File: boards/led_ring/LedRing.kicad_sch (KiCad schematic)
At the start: 34 parts, among them J10 FH12-6S-0.5SH(55)

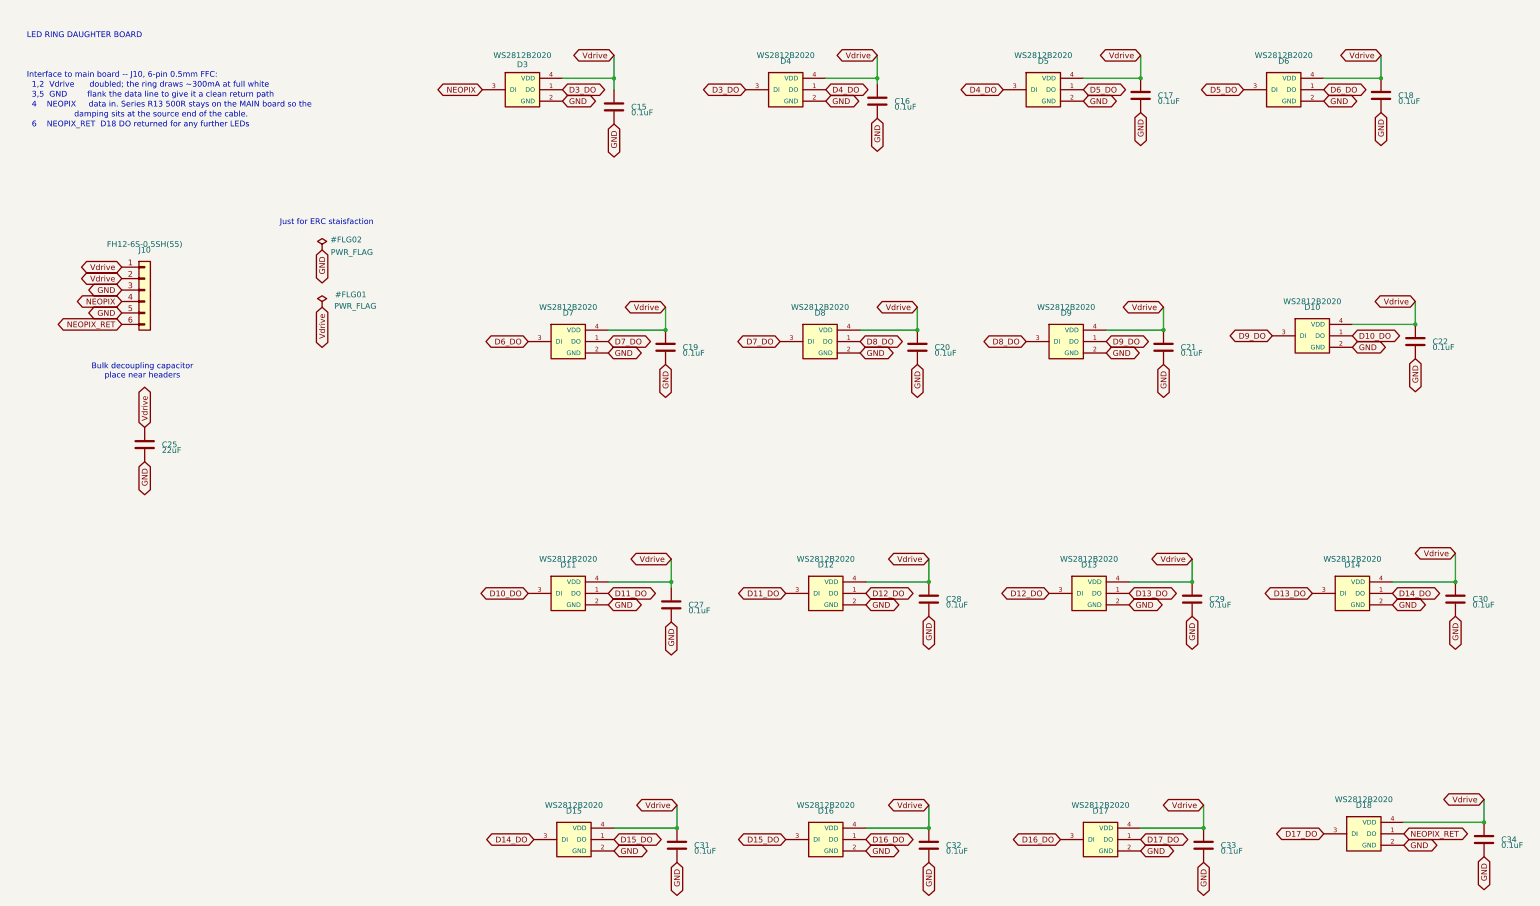
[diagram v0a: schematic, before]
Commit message: Board migrations. Move to newer LED and IMU
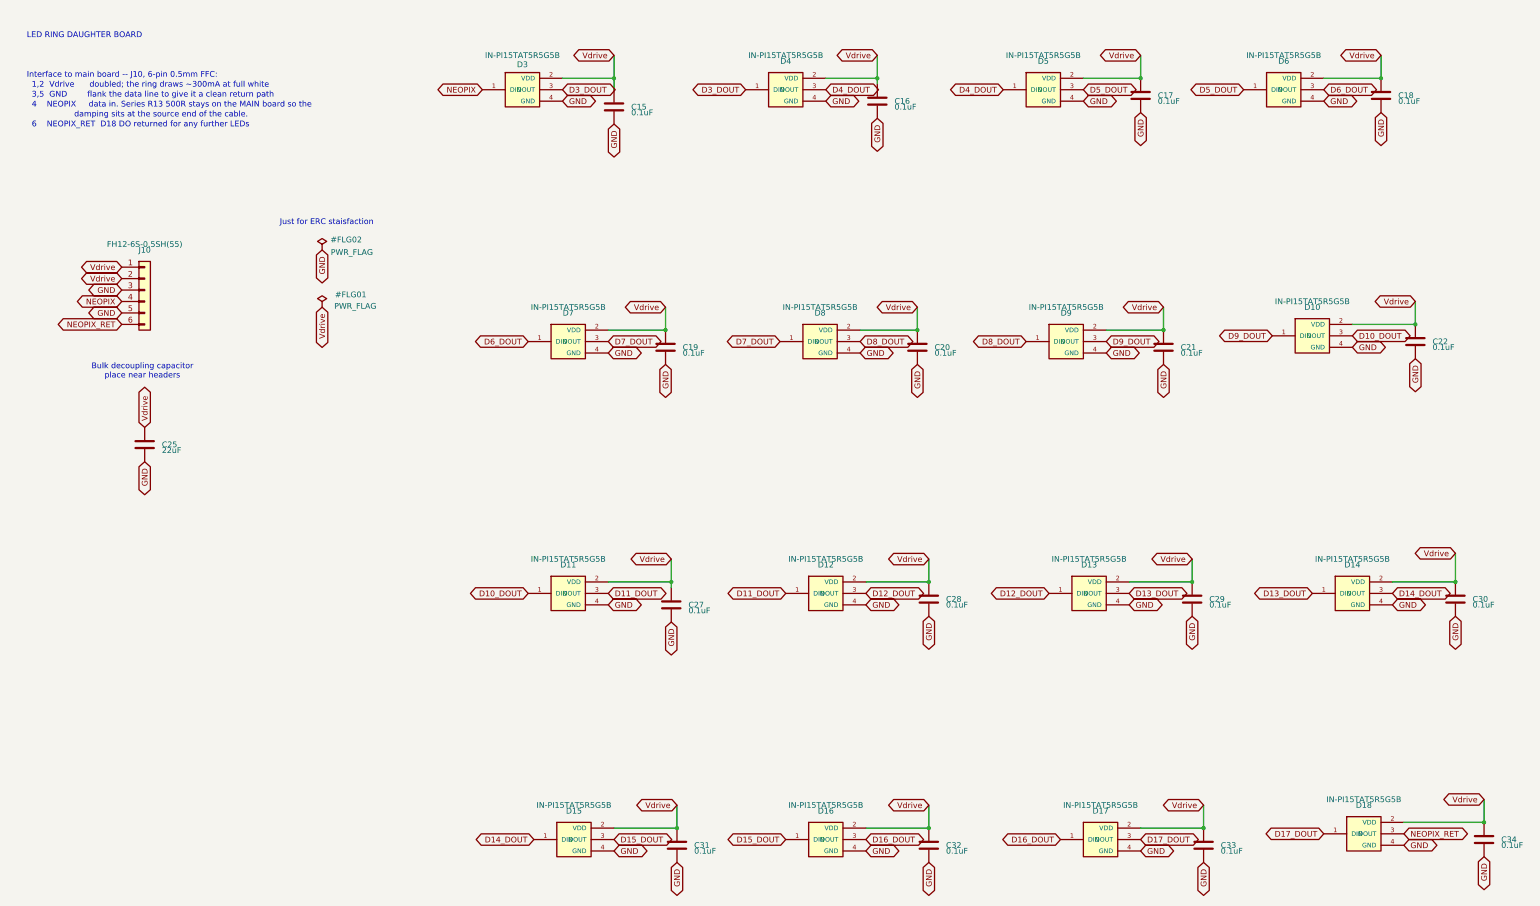
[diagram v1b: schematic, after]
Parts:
- C15, C16, C17, C18, C19, C20, C21, C22, C27, C28, C29, C30, C31, C32, C33, C34: Dielectric (none) -> X7R; DigiKey_PN (none) -> 1276-6844-1-ND; MPN (none) -> CL05B104KO5VPNC; Manufacturer (none) -> Samsung Electro-Mechanics; Voltage (none) -> 16V
- C25: Dielectric (none) -> X5R; DigiKey_PN (none) -> 1276-6786-1-ND; MPN (none) -> CL21A226KPCLRNC; Manufacturer (none) -> Samsung Electro-Mechanics; Voltage (none) -> 10V
- D10, D11, D12, D13, D14, D15, D16, D17, D4, D5, D6, D7, D8, D9: value WS2812B2020 -> IN-PI15TAT5R5G5B; footprint smart_compass:LED_WS2812B2020 -> smart_compass:LED_Inolux_IN-PI15TAT5R5G5B_1515; symbol smart_compass:WS2812B2020 -> smart_compass:IN-PI15TAT5R5G5B; DigiKey_PN (none) -> 1830-IN-PI15TAT5R5G5BCT-ND; MPN (none) -> IN-PI15TAT5R5G5B; Manufacturer (none) -> Inolux
- D18: value WS2812B2020 -> IN-PI15TAT5R5G5B; footprint smart_compass:LED_WS2812B2020 -> smart_compass:LED_Inolux_IN-PI15TAT5R5G5B_1515; symbol smart_compass:WS2812B2020 -> smart_compass:IN-PI15TAT5R5G5B; DigiKey_PN (none) -> 1830-IN-PI15TAT5R5G5BCT-ND; MPN (none) -> IN-PI15TAT5R5G5B; Manufacturer (none) -> Inolux; Sourcing_Note (none) -> Chain DOUT returns to the main board as NEOPIX_RET. The Ino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
- D3: value WS2812B2020 -> IN-PI15TAT5R5G5B; footprint smart_compass:LED_WS2812B2020 -> smart_compass:LED_Inolux_IN-PI15TAT5R5G5B_1515; symbol smart_compass:WS2812B2020 -> smart_compass:IN-PI15TAT5R5G5B; DigiKey_PN (none) -> 1830-IN-PI15TAT5R5G5BCT-ND; MPN (none) -> IN-PI15TAT5R5G5B; Manufacturer (none) -> Inolux; Sourcing_Note (none) -> V_IH is specified as 3.4V absolute at VDD=5.0V, NOT as a ra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
- J10: DigiKey_PN (none) -> HFJ106CT-ND; MPN (none) -> FH12-6S-0.5SH(55); Manufacturer (none) -> Hirose Electric Co Ltd; Sourcing_Note (none) -> Digi-Key stock 0, 16-week factory lead. Must be resolved to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
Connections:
- net GND: now also D10.4 (GND), D11.4 (GND), D12.4 (GND), D13.4 (GND), D14.4 (GND), D15.4 (GND), D16.4 (GND), D17.4 (GND), D18.4 (GND), D3.4 (GND), D4.4 (GND), D5.4 (GND), D6.4 (GND), D7.4 (GND), D8.4 (GND), D9.4 (GND); no longer D10.2 (GND), D11.2 (GND), D12.2 (GND), D13.2 (GND), D14.2 (GND), D15.2 (GND), D16.2 (GND), D17.2 (GND), D18.2 (GND), D3.2 (GND), D4.2 (GND), D5.2 (GND), D6.2 (GND), D7.2 (GND), D8.2 (GND), D9.2 (GND)
- net NEOPIX: now also D3.1 (DIN); no longer D3.3 (DI)
- net NEOPIX_RET: now also D18.3 (DOUT); no longer D18.1 (DO)
- net Vdrive: now also D10.2 (VDD), D11.2 (VDD), D12.2 (VDD), D13.2 (VDD), D14.2 (VDD), D15.2 (VDD), D16.2 (VDD), D17.2 (VDD), D18.2 (VDD), D3.2 (VDD), D4.2 (VDD), D5.2 (VDD), D6.2 (VDD), D7.2 (VDD), D8.2 (VDD), D9.2 (VDD); no longer D10.4 (VDD), D11.4 (VDD), D12.4 (VDD), D13.4 (VDD), D14.4 (VDD), D15.4 (VDD), D16.4 (VDD), D17.4 (VDD), D18.4 (VDD), D3.4 (VDD), D4.4 (VDD), D5.4 (VDD), D6.4 (VDD), D7.4 (VDD), D8.4 (VDD), D9.4 (VDD)
- net D10_DO renamed D11_DOUT
- net D11_DOUT: now also D12.1 (DIN); no longer D10.1 (DO)
- net D11_DO renamed D10_DOUT
- net D10_DOUT: now also D10.3 (DOUT); no longer D12.3 (DI)
- net D12_DO renamed D13_DOUT
- net D13_DOUT: now also D14.1 (DIN); no longer D12.1 (DO)
- net D13_DO renamed D12_DOUT
- net D12_DOUT: now also D12.3 (DOUT); no longer D14.3 (DI)
- net D14_DO renamed D15_DOUT
- net D15_DOUT: now also D16.1 (DIN); no longer D14.1 (DO)
- net D15_DO renamed D14_DOUT
- net D14_DOUT: now also D14.3 (DOUT); no longer D16.3 (DI)
- net D16_DO renamed D17_DOUT
- net D17_DOUT: now also D18.1 (DIN); no longer D16.1 (DO)
- net D17_DO renamed D16_DOUT
- net D16_DOUT: now also D16.3 (DOUT); no longer D18.3 (DI)
- net D3_DO renamed D4_DOUT
- net D4_DOUT: now also D5.1 (DIN); no longer D3.1 (DO)
- net D4_DO renamed D3_DOUT
- net D3_DOUT: now also D3.3 (DOUT); no longer D5.3 (DI)
- net D5_DO renamed D6_DOUT
- net D6_DOUT: now also D7.1 (DIN); no longer D5.1 (DO)
- net D6_DO renamed D5_DOUT
- net D5_DOUT: now also D5.3 (DOUT); no longer D7.3 (DI)
- net D7_DO renamed D8_DOUT
- net D8_DOUT: now also D9.1 (DIN); no longer D7.1 (DO)
- net D8_DO renamed D7_DOUT
- net D7_DOUT: now also D7.3 (DOUT); no longer D9.3 (DI)
- removed net D9_DO: D10.3 (DI), D9.1 (DO)
- new net D9_DOUT: D10.1 (DIN), D9.3 (DOUT)

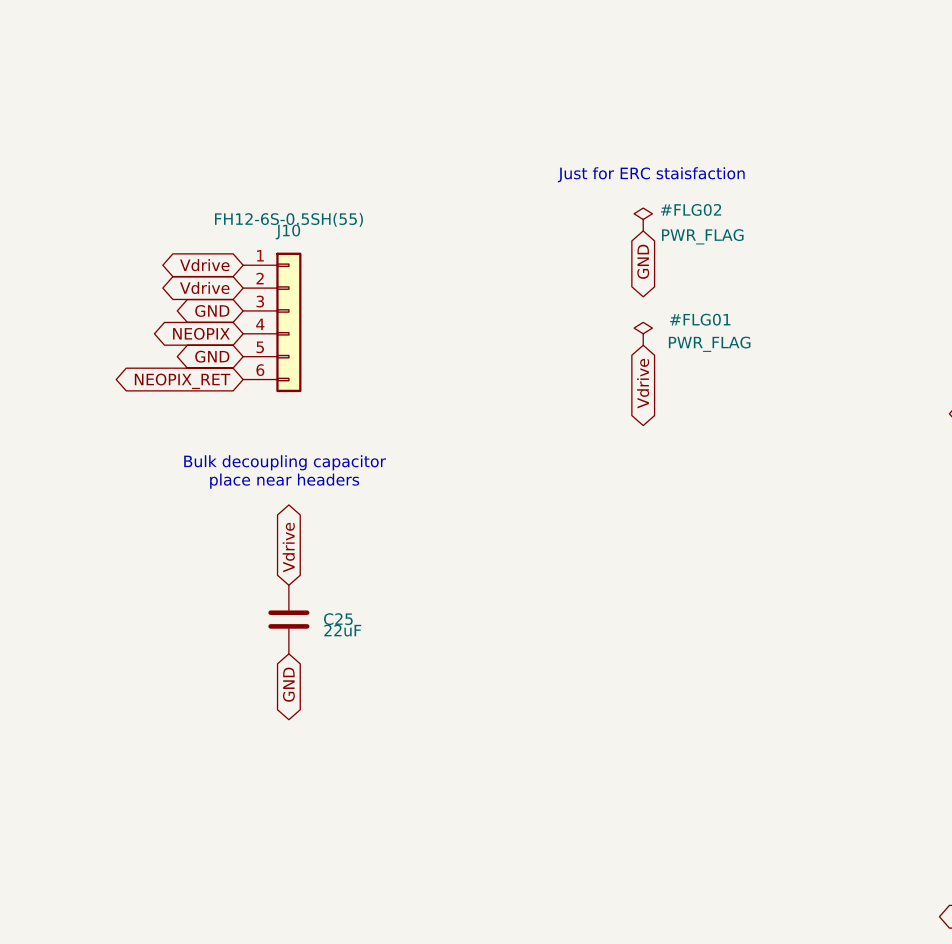
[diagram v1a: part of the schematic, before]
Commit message: some more component reworking. Moved to 10 lane ribbon connects between all boards
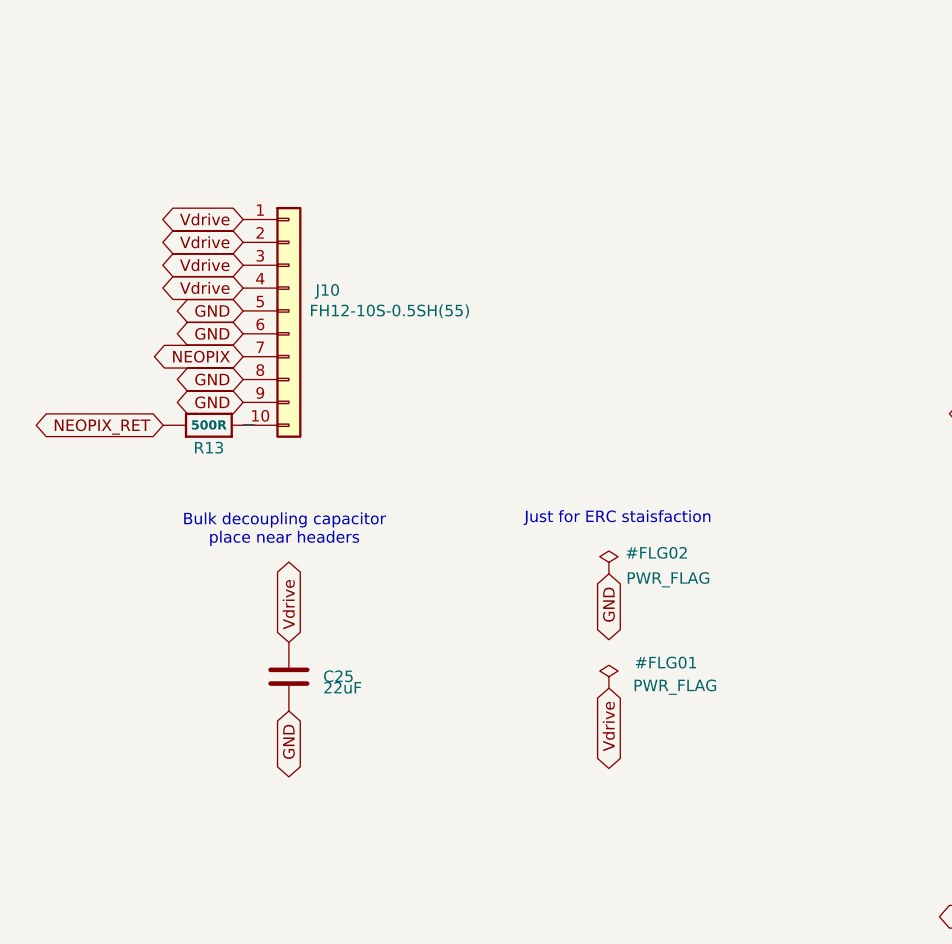
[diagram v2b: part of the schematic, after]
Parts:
- removed J10: FH12-6S-0.5SH(55), Connector_FFC-FPC:Hirose_FH12-6S-0.5SH_1x06-1MP_P0.50mm_Horizontal, symbol Connector_Generic:Conn_01x06
- added J10: FH12-10S-0.5SH(55), Connector_FFC-FPC:Hirose_FH12-10S-0.5SH_1x10-1MP_P0.50mm_Horizontal, symbol Connector_Generic:Conn_01x10
- added R13: 500R, Resistor_SMD:R_0603_1608Metric, symbol smart_compass_main:RESISTOR_0603_NOOUT
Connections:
- net GND: now also J10.5 (Pin_5), J10.6 (Pin_6), J10.8 (Pin_8), J10.9 (Pin_9)
- net NEOPIX: now also J10.7 (Pin_7)
- net NEOPIX_RET: now also R13.2
- net Vdrive: now also J10.1 (Pin_1), J10.2 (Pin_2), J10.3 (Pin_3), J10.4 (Pin_4)
- new net: J10.10 (Pin_10), R13.1
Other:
- moved on the sheet: C25
